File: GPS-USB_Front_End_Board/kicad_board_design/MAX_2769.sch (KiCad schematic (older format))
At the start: 50 parts, among them J3 SMA, P2 CONN_01X03, U4 MAX8510, U5 MAX8510, U6 MAX2771, U7 SAWTEK-855969, U8 LT1719S6 -- Not Populated, X1 13.368MHz TCXO

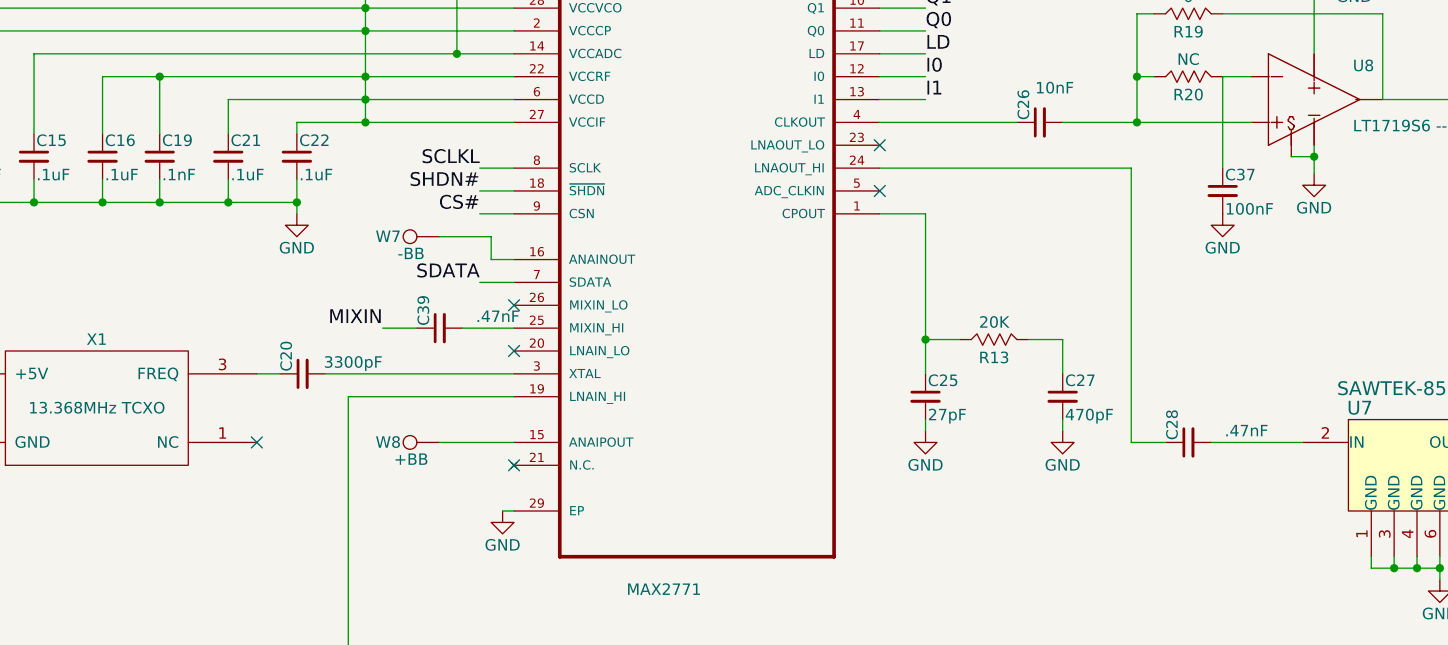
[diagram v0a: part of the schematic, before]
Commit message: Fix value display on EEPROM.  Consolidate some part values.
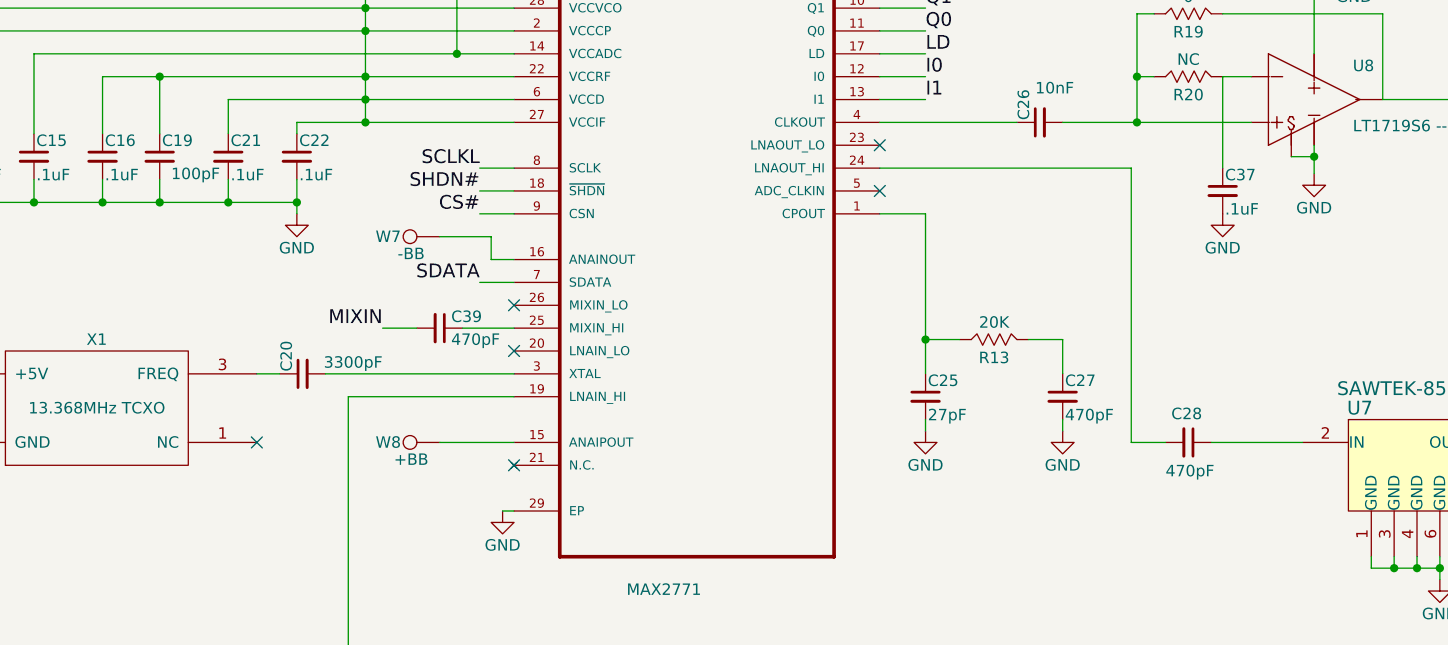
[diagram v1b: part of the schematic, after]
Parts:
- C19: value .1nF -> 100pF; MFR Kemet -> Yageo; MPN C0805C101K4RAC7800 -> CC0402JRNPO9BN101; SPN 399-15003-1-ND -> 311-1024-1-ND
- C28, C39: value .47nF -> 470pF
- C37: value 100nF -> .1uF
- P2: MFR (none) -> Sullins; MPN (none) -> PREC003SAAN-RC; SPN (none) -> S1012EC-03-ND; SPR (none) -> Digikey
- U6: MFR (none) -> Maxim; MPN (none) -> MAX2771ETI+; SPN (none) -> MAX2771ETI+-ND; SPR (none) -> Digikey
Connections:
- net MIXIN: now also C39.2; no longer C39.1
- net at C28.1: now also U7.2 (IN); no longer U6.24 (LNAOUT_HI)
- net at C28.2: now also U6.24 (LNAOUT_HI); no longer U7.2 (IN)
- net at U6.25 (MIXIN_HI): now also C39.1; no longer C39.2
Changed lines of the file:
@@
-$EndComp
-$Comp
-L C_Small C19
-U 1 1 5B222EB0
-P 4325 1900
-F 0 "C19" H 4335 1970 50  0000 L CNN
-F 1 ".1nF" H 4335 1820 50  0000 L CNN
-F 2 "Capacitors_SMD:C_0402" H 4325 1900 50  0001 C CNN
-F 3 "" H 4325 1900 50  0001 C CNN
-F 4 "Kemet" H 0   0   50  0001 C CNN "MFR"
-F 5 "C0805C101K4RAC7800" H 0   0   50  0001 C CNN "MPN"
-F 6 "Digikey" H 0   0   50  0001 C CNN "SPR"
-F 7 "399-15003-1-ND" H 0   0   50  0001 C CNN "SPN"
-F 8 "-" H 0   0   50  0001 C CNN "SPURL"
-	1    4325 1900
-	1    0    0    -1
 $EndComp
 $Comp
@@
 	1    4925 2150
 	1    0    0    -1
-$EndComp
-$Comp
-L C_Small C28
-U 1 1 5B223AF8
-P 8825 3150
-F 0 "C28" H 8835 3220 50  0000 L CNN
-F 1 ".47nF" V 8875 2800 50  0000 L CNN
-F 2 "Capacitors_SMD:C_0402" H 8825 3150 50  0001 C CNN
-F 3 "" H 8825 3150 50  0001 C CNN
-F 4 "AVX" H 0   0   50  0001 C CNN "MFR"
-F 5 "04025C471KAT2A" H 0   0   50  0001 C CNN "MPN"
-F 6 "Digikey" H 0   0   50  0001 C CNN "SPR"
-F 7 "478-1097-1-ND" H 0   0   50  0001 C CNN "SPN"
-F 8 "-" H 0   0   50  0001 C CNN "SPURL"
-	1    8825 3150
-	0    -1   -1   0
 $EndComp
 $Comp
@@
 	1    8825 1550
 	0    1    1    0
-$EndComp
-$Comp
-L C_Small C37
-U 1 1 5B5EA13E
-P 8975 2050
-F 0 "C37" H 8985 2120 50  0000 L CNN
-F 1 "100nF" H 8985 1970 50  0000 L CNN
-F 2 "Capacitors_SMD:C_0402" H 8975 2050 50  0001 C CNN
-F 3 "" H 8975 2050 50  0001 C CNN
-F 4 "TDK" H 0   0   50  0001 C CNN "MFR"
-F 5 "CGA2B1X7R1C104K050BC" H 0   0   50  0001 C CNN "MPN"
-F 6 "Digikey" H 0   0   50  0001 C CNN "SPR"
-F 7 "445-5613-1-ND" H 0   0   50  0001 C CNN "SPN"
-F 8 "-" H 0   0   50  0001 C CNN "SPURL"
-	1    8975 2050
-	1    0    0    -1
 $EndComp
 $Comp
@@
 F 7 "Maxim Integrated" H 6675 2250 50  0001 L BNN "Field7"
 F 8 "TQFN-28 Maxim Integrated" H 6675 2250 50  0001 L BNN "Field8"
+F 9 "Maxim" H 6675 2250 60  0001 C CNN "MFR"
+F 10 "Digikey" H 6675 2250 60  0001 C CNN "SPR"
+F 11 "MAX2771ETI+-ND" H 6675 2250 60  0001 C CNN "SPN"
+F 12 "MAX2771ETI+" H 6675 2250 60  0001 C CNN "MPN"
 	1    6675 2250
 	1    0    0    -1
@@
 F 2 "Connectors_Molex:Molex_KK-6410-03_03x2.54mm_Straight" H 2450 6275 50  0001 C CNN
 F 3 "" H 2450 6275 50  0000 C CNN
+F 4 "Sullins" H 2450 6275 60  0001 C CNN "MFR"
+F 5 "PREC003SAAN-RC" H 2450 6275 60  0001 C CNN "MPN"
+F 6 "Digikey" H 2450 6275 60  0001 C CNN "SPR"
+F 7 "S1012EC-03-ND" H 2450 6275 60  0001 C CNN "SPN"
 	1    2450 6275
 	-1   0    0    1
@@
 	2700 6175 2700 5900
 $Comp
-L C_Small C39
-U 1 1 5D3D9921
-P 5550 2650
-F 0 "C39" H 5560 2720 50  0000 L CNN
-F 1 ".47nF" V 5600 2300 50  0000 L CNN
-F 2 "Capacitors_SMD:C_0402" H 5550 2650 50  0001 C CNN
-F 3 "" H 5550 2650 50  0001 C CNN
-F 4 "AVX" H -3275 -500 50  0001 C CNN "MFR"
-F 5 "04025C471KAT2A" H -3275 -500 50  0001 C CNN "MPN"
-F 6 "Digikey" H -3275 -500 50  0001 C CNN "SPR"
-F 7 "478-1097-1-ND" H -3275 -500 50  0001 C CNN "SPN"
-F 8 "-" H -3275 -500 50  0001 C CNN "SPURL"
-	1    5550 2650
-	0    -1   -1   0
-$EndComp
-$Comp
 L C_Small C31
 U 1 1 5D3DDB42
@@
 	1    0    0    -1
 $EndComp
+$Comp
+L C_Small C19
+U 1 1 5D445DBF
+P 4325 1900
+F 0 "C19" H 4335 1970 50  0000 L CNN
+F 1 "100pF" H 4375 1825 50  0000 L CNN
+F 2 "Capacitors_SMD:C_0402" H 4325 1900 50  0001 C CNN
+F 3 "" H 4325 1900 50  0001 C CNN
+F 4 "Yageo" H -625 -3475 50  0001 C CNN "MFR"
+F 5 "CC0402JRNPO9BN101" H -625 -3475 50  0001 C CNN "MPN"
+F 6 "Digikey" H -625 -3475 50  0001 C CNN "SPR"
+F 7 "311-1024-1-ND" H -625 -3475 50  0001 C CNN "SPN"
+F 8 "-" H -625 -3475 50  0001 C CNN "SPURL"
+	1    4325 1900
+	1    0    0    -1
+$EndComp
+$Comp
+L C_Small C39
+U 1 1 5D447C40
+P 5550 2650
+F 0 "C39" V 5500 2700 50  0000 L CNN
+F 1 "470pF" V 5600 2700 50  0000 L CNN
+F 2 "Capacitors_SMD:C_0402" H 5550 2650 50  0001 C CNN
+F 3 "" H 5550 2650 50  0001 C CNN
+F 4 "AVX" H -2725 -300 50  0001 C CNN "MFR"
+F 5 "04025C471KAT2A" H -2725 -300 50  0001 C CNN "MPN"
+F 6 "Digikey" H -2725 -300 50  0001 C CNN "SPR"
+F 7 "478-1097-1-ND" H -2725 -300 50  0001 C CNN "SPN"
+F 8 "-" H -2725 -300 50  0001 C CNN "SPURL"
+	1    5550 2650
+	0    1    1    0
+$EndComp
+$Comp
+L C_Small C28
+U 1 1 5D447FCE
+P 8825 3150
+F 0 "C28" V 8700 3075 50  0000 L CNN
+F 1 "470pF" V 8950 3050 50  0000 L CNN
+F 2 "Capacitors_SMD:C_0402" H 8825 3150 50  0001 C CNN
+F 3 "" H 8825 3150 50  0001 C CNN
+F 4 "AVX" H 550 200 50  0001 C CNN "MFR"
+F 5 "04025C471KAT2A" H 550 200 50  0001 C CNN "MPN"
+F 6 "Digikey" H 550 200 50  0001 C CNN "SPR"
+F 7 "478-1097-1-ND" H 550 200 50  0001 C CNN "SPN"
+F 8 "-" H 550 200 50  0001 C CNN "SPURL"
+	1    8825 3150
+	0    1    1    0
+$EndComp
+$Comp
+L C_Small C37
+U 1 1 5D44AA0F
+P 8975 2050
+F 0 "C37" H 8985 2120 50  0000 L CNN
+F 1 ".1uF" H 8985 1970 50  0000 L CNN
+F 2 "Capacitors_SMD:C_0402" H 8975 2050 50  0001 C CNN
+F 3 "" H 8975 2050 50  0001 C CNN
+F 4 "TDK" H 4050 150 50  0001 C CNN "MFR"
+F 5 "CGA2B1X7R1C104K050BC" H 4050 150 50  0001 C CNN "MPN"
+F 6 "Digikey" H 4050 150 50  0001 C CNN "SPR"
+F 7 "445-5613-1-ND" H 4050 150 50  0001 C CNN "SPN"
+F 8 "-" H 4050 150 50  0001 C CNN "SPURL"
+	1    8975 2050
+	1    0    0    -1
+$EndComp

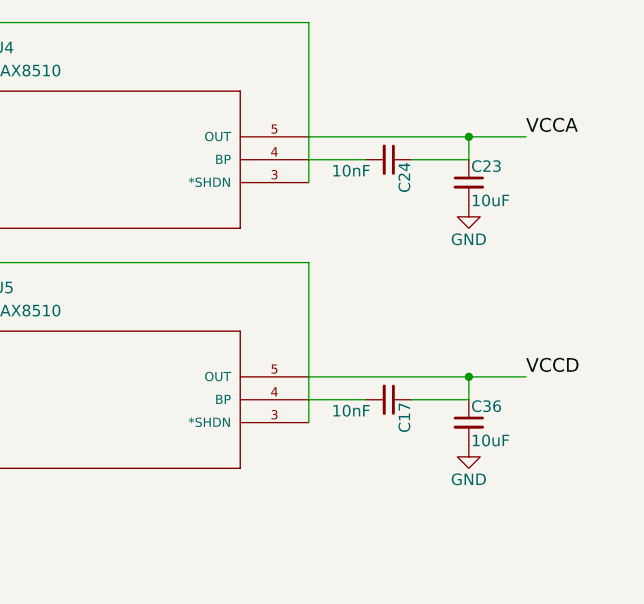
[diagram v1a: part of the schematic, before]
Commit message: Run DRC, generate and import netlist w/ new caps.
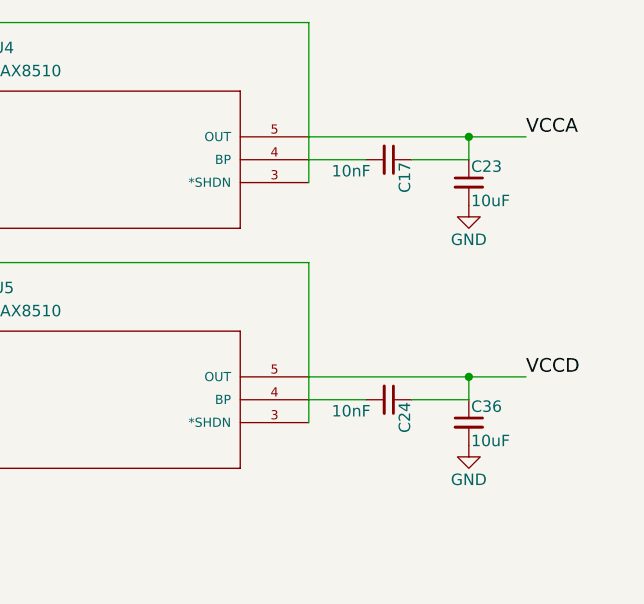
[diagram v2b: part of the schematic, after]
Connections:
- net VCCA: now also C17.1; no longer C24.1
- net VCCD: now also C24.1; no longer C17.1
- net at U4.4 (BP): now also C17.2; no longer C24.2
- net at U5.4 (BP): now also C24.2; no longer C17.2
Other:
- moved on the sheet: C17, C24
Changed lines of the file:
@@
 $EndComp
 $Comp
-L GND #PWR023
+L GND #PWR025
 U 1 1 5B222B6C
 P 3200 3250
-F 0 "#PWR023" H 3200 3000 50  0001 C CNN
+F 0 "#PWR025" H 3200 3000 50  0001 C CNN
 F 1 "GND" H 3200 3100 50  0000 C CNN
 F 2 "" H 3200 3250 50  0000 C CNN
@@
 $EndComp
 $Comp
-L GND #PWR024
+L GND #PWR026
 U 1 1 5B223315
 P 4925 2150
-F 0 "#PWR024" H 4925 1900 50  0001 C CNN
+F 0 "#PWR026" H 4925 1900 50  0001 C CNN
 F 1 "GND" H 4925 2000 50  0000 C CNN
 F 2 "" H 4925 2150 50  0000 C CNN
@@
 $EndComp
 $Comp
-L GND #PWR025
+L GND #PWR027
 U 1 1 5B2243D4
 P 8275 3100
-F 0 "#PWR025" H 8275 2850 50  0001 C CNN
+F 0 "#PWR027" H 8275 2850 50  0001 C CNN
 F 1 "GND" H 8275 2950 50  0000 C CNN
 F 2 "" H 8275 3100 50  0000 C CNN
@@
 $EndComp
 $Comp
-L GND #PWR026
+L GND #PWR028
 U 1 1 5B224439
 P 7675 3100
-F 0 "#PWR026" H 7675 2850 50  0001 C CNN
+F 0 "#PWR028" H 7675 2850 50  0001 C CNN
 F 1 "GND" H 7675 2950 50  0000 C CNN
 F 2 "" H 7675 3100 50  0000 C CNN
@@
 $EndComp
 $Comp
-L GND #PWR027
+L GND #PWR029
 U 1 1 5B238E15
 P 5825 3450
-F 0 "#PWR027" H 5825 3200 50  0001 C CNN
+F 0 "#PWR029" H 5825 3200 50  0001 C CNN
 F 1 "GND" H 5825 3300 50  0000 C CNN
 F 2 "" H 5825 3450 50  0000 C CNN
@@
 $EndComp
 $Comp
-L GND #PWR028
+L GND #PWR030
 U 1 1 5B239878
 P 3300 5875
-F 0 "#PWR028" H 3300 5625 50  0001 C CNN
+F 0 "#PWR030" H 3300 5625 50  0001 C CNN
 F 1 "GND" H 3300 5725 50  0000 C CNN
 F 2 "" H 3300 5875 50  0000 C CNN
@@
 $EndComp
 $Comp
-L GND #PWR029
+L GND #PWR031
 U 1 1 5B23B5B2
 P 3200 6675
-F 0 "#PWR029" H 3200 6425 50  0001 C CNN
+F 0 "#PWR031" H 3200 6425 50  0001 C CNN
 F 1 "GND" H 3200 6525 50  0000 C CNN
 F 2 "" H 3200 6675 50  0000 C CNN
@@
 $EndComp
 $Comp
-L GND #PWR030
+L GND #PWR032
 U 1 1 5B23DBFD
 P 9925 3750
-F 0 "#PWR030" H 9925 3500 50  0001 C CNN
+F 0 "#PWR032" H 9925 3500 50  0001 C CNN
 F 1 "GND" H 9925 3600 50  0000 C CNN
 F 2 "" H 9925 3750 50  0000 C CNN
@@
 $EndComp
 $Comp
-L GND #PWR031
+L GND #PWR033
 U 1 1 5B2B7669
 P 7025 5100
-F 0 "#PWR031" H 7025 4850 50  0001 C CNN
+F 0 "#PWR033" H 7025 4850 50  0001 C CNN
 F 1 "GND" H 7025 4950 50  0000 C CNN
 F 2 "" H 7025 5100 50  0000 C CNN
@@
 $EndComp
 $Comp
-L GND #PWR032
+L GND #PWR034
 U 1 1 5B2B7730
 P 7375 4850
-F 0 "#PWR032" H 7375 4600 50  0001 C CNN
+F 0 "#PWR034" H 7375 4600 50  0001 C CNN
 F 1 "GND" H 7375 4700 50  0000 C CNN
 F 2 "" H 7375 4850 50  0000 C CNN
@@
 $EndComp
 $Comp
-L GND #PWR033
+L GND #PWR035
 U 1 1 5B2B78BD
 P 10475 5050
-F 0 "#PWR033" H 10475 4800 50  0001 C CNN
+F 0 "#PWR035" H 10475 4800 50  0001 C CNN
 F 1 "GND" H 10475 4900 50  0000 C CNN
 F 2 "" H 10475 5050 50  0000 C CNN
@@
 $EndComp
 $Comp
-L GND #PWR034
+L GND #PWR036
 U 1 1 5B2B8EC4
 P 1825 4700
-F 0 "#PWR034" H 1825 4450 50  0001 C CNN
+F 0 "#PWR036" H 1825 4450 50  0001 C CNN
 F 1 "GND" H 1825 4550 50  0000 C CNN
 F 2 "" H 1825 4700 50  0000 C CNN
@@
 L C_Small C24
 U 1 1 5B5DF4D0
-P 10125 4850
-F 0 "C24" H 10135 4920 50  0000 L CNN
-F 1 "10nF" V 10175 4600 50  0000 L CNN
-F 2 "Capacitors_SMD:C_0402" H 10125 4850 50  0001 C CNN
-F 3 "" H 10125 4850 50  0001 C CNN
-F 4 "Murata" H 0   0   50  0001 C CNN "MFR"
-F 5 "GRM155R71C103KA01D" H 0   0   50  0001 C CNN "MPN"
-F 6 "Digikey" H 0   0   50  0001 C CNN "SPR"
-F 7 "490-1313-1-ND" H 0   0   50  0001 C CNN "SPN"
-F 8 "-" H 0   0   50  0001 C CNN "SPURL"
-	1    10125 4850
+P 10125 5900
+F 0 "C24" H 10135 5970 50  0000 L CNN
+F 1 "10nF" V 10175 5650 50  0000 L CNN
+F 2 "Capacitors_SMD:C_0402" H 10125 5900 50  0001 C CNN
+F 3 "" H 10125 5900 50  0001 C CNN
+F 4 "Murata" H 0   1050 50  0001 C CNN "MFR"
+F 5 "GRM155R71C103KA01D" H 0   1050 50  0001 C CNN "MPN"
+F 6 "Digikey" H 0   1050 50  0001 C CNN "SPR"
+F 7 "490-1313-1-ND" H 0   1050 50  0001 C CNN "SPN"
+F 8 "-" H 0   1050 50  0001 C CNN "SPURL"
+	1    10125 5900
 	0    1    1    0
 $EndComp
@@
 $EndComp
 $Comp
-L GND #PWR035
+L GND #PWR037
 U 1 1 5B5E0589
 P 7025 6150
-F 0 "#PWR035" H 7025 5900 50  0001 C CNN
+F 0 "#PWR037" H 7025 5900 50  0001 C CNN
 F 1 "GND" H 7025 6000 50  0000 C CNN
 F 2 "" H 7025 6150 50  0000 C CNN
@@
 $EndComp
 $Comp
-L GND #PWR036
+L GND #PWR038
 U 1 1 5B5E058F
 P 7375 5900
-F 0 "#PWR036" H 7375 5650 50  0001 C CNN
+F 0 "#PWR038" H 7375 5650 50  0001 C CNN
 F 1 "GND" H 7375 5750 50  0000 C CNN
 F 2 "" H 7375 5900 50  0000 C CNN
@@
 $EndComp
 $Comp
-L GND #PWR037
+L GND #PWR039
 U 1 1 5B5E0595
 P 10475 6100
-F 0 "#PWR037" H 10475 5850 50  0001 C CNN
+F 0 "#PWR039" H 10475 5850 50  0001 C CNN
 F 1 "GND" H 10475 5950 50  0000 C CNN
 F 2 "" H 10475 6100 50  0000 C CNN
@@
 L C_Small C17
 U 1 1 5B5E05AD
-P 10125 5900
-F 0 "C17" H 10135 5970 50  0000 L CNN
-F 1 "10nF" V 10175 5650 50  0000 L CNN
-F 2 "Capacitors_SMD:C_0402" H 10125 5900 50  0001 C CNN
-F 3 "" H 10125 5900 50  0001 C CNN
-F 4 "Murata" H 0   0   50  0001 C CNN "MFR"
-F 5 "GRM155R71C103KA01D" H 0   0   50  0001 C CNN "MPN"
-F 6 "Digikey" H 0   0   50  0001 C CNN "SPR"
-F 7 "490-1313-1-ND" H 0   0   50  0001 C CNN "SPN"
-F 8 "-" H 0   0   50  0001 C CNN "SPURL"
-	1    10125 5900
+P 10125 4850
+F 0 "C17" H 10135 4920 50  0000 L CNN
+F 1 "10nF" V 10175 4600 50  0000 L CNN
+F 2 "Capacitors_SMD:C_0402" H 10125 4850 50  0001 C CNN
+F 3 "" H 10125 4850 50  0001 C CNN
+F 4 "Murata" H 0   -1050 50  0001 C CNN "MFR"
+F 5 "GRM155R71C103KA01D" H 0   -1050 50  0001 C CNN "MPN"
+F 6 "Digikey" H 0   -1050 50  0001 C CNN "SPR"
+F 7 "490-1313-1-ND" H 0   -1050 50  0001 C CNN "SPN"
+F 8 "-" H 0   -1050 50  0001 C CNN "SPURL"
+	1    10125 4850
 	0    1    1    0
 $EndComp
@@
 $EndComp
 $Comp
-L GND #PWR038
+L GND #PWR040
 U 1 1 5B5EA299
 P 8975 2150
-F 0 "#PWR038" H 8975 1900 50  0001 C CNN
+F 0 "#PWR040" H 8975 1900 50  0001 C CNN
 F 1 "GND" H 8975 2000 50  0000 C CNN
 F 2 "" H 8975 2150 50  0000 C CNN
@@
 $EndComp
 $Comp
-L GND #PWR039
+L GND #PWR041
 U 1 1 5B5EAC9C
 P 9375 1975
-F 0 "#PWR039" H 9375 1725 50  0001 C CNN
+F 0 "#PWR041" H 9375 1725 50  0001 C CNN
 F 1 "GND" H 9375 1825 50  0000 C CNN
 F 2 "" H 9375 1975 50  0000 C CNN
@@
 $EndComp
 $Comp
-L GND #PWR040
+L GND #PWR042
 U 1 1 5B5EE330
 P 9550 1050
-F 0 "#PWR040" H 9550 800 50  0001 C CNN
+F 0 "#PWR042" H 9550 800 50  0001 C CNN
 F 1 "GND" H 9550 900 50  0000 C CNN
 F 2 "" H 9550 1050 50  0000 C CNN
@@
 $EndComp
 $Comp
-L GND #PWR041
+L GND #PWR043
 U 1 1 5D3C1AC7
 P 4400 6100
-F 0 "#PWR041" H 4400 5850 50  0001 C CNN
+F 0 "#PWR043" H 4400 5850 50  0001 C CNN
 F 1 "GND" H 4400 5950 50  0000 C CNN
 F 2 "" H 4400 6100 50  0000 C CNN
